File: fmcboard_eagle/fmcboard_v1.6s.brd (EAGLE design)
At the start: 147 x 74 mm, 294 parts, among them IC1 OPA699ID, IC10 LM358, IC11 7805DT, IC12 SN74AUC2G66DCTR, IC13 SN74AUC2G66DCTR, IC14 SN74AUC2G66DCTR, IC15 SN74AUC2G66DCTR, IC16 DAC7578SPWR, IC17 SN74AUC2G66DCTR, IC18 SN74AUC2G66DCTR, IC19 SN74AUC2G66DCTR, IC2 DAC7578SPWR, IC20 SN74AUC2G66DCTR, IC21 74AUP2GU04GW, IC22 74AUP2GU04GW, IC23 74AUP2GU04GW, IC24 74AUP2GU04GW, IC25 MC7905ACD2TR4G, IC26 AMS1117-1.8, IC27 LM358, IC28 SN74AUC2G66DCTR, IC29 LM337KVURG3, IC3 LTC6229IMS8E#TRPBF, IC30 SN74AUC2G66DCTR, IC31 SN74AUC2G66DCTR, IC32 SN74AUC2G66DCTR, IC33 LTC6229IMS8E#TRPBF, IC34 74AUP2GU04GW, IC35 74AUP2GU04GW, IC36 TPS5430DDAR, IC37 TPS5430DDAR, IC4 OPA695IDR, IC5 LTC6229IMS8E#TRPBF, IC6 OPA695IDR, IC7 OPA699ID, IC8 LM358, IC9 LM358, J1 8pin, J12 4p-2.54, J13 4p-2.54, J2 ASP-134604-01, J3 2p-2.54, J5 4p-2.54, J8 4p-2.54, J9 2p-2.54

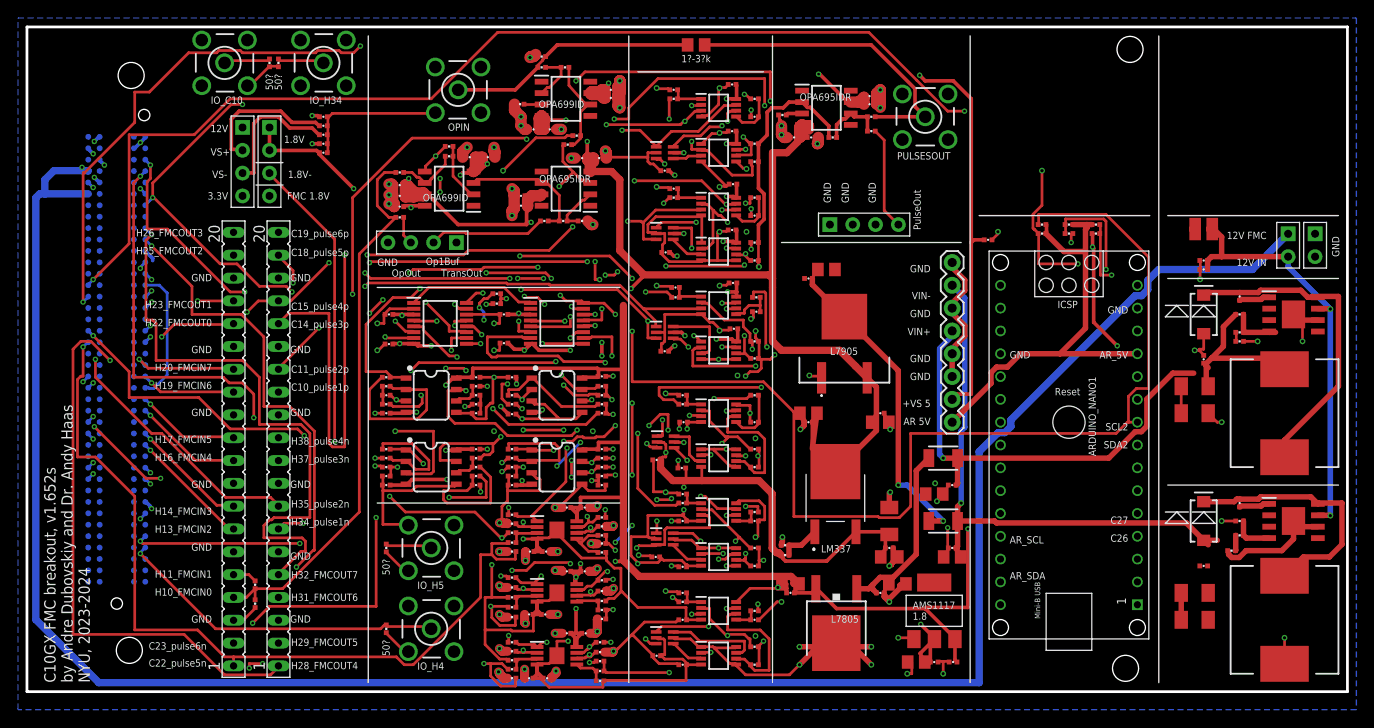
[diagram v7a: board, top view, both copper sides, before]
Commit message: 0805 10uF
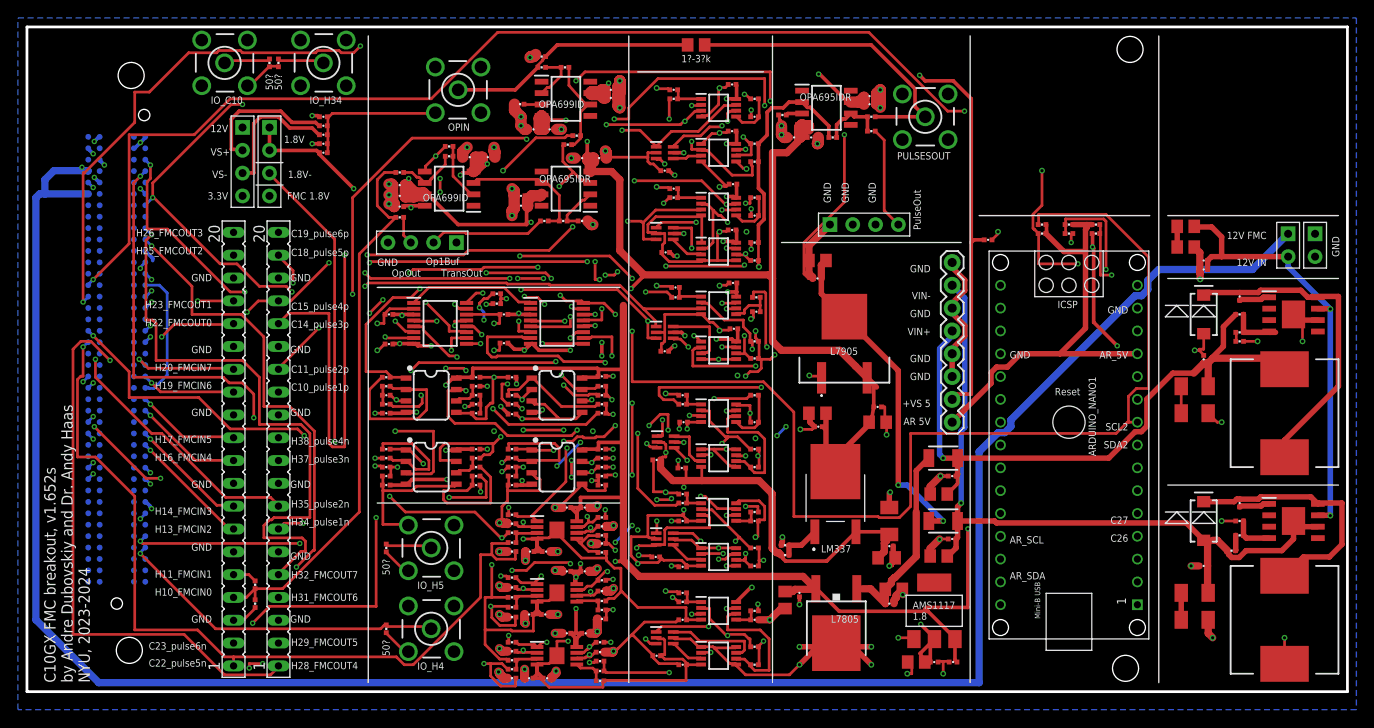
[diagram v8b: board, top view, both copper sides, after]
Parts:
- moved C120 2.50 mm to (129.0, 49.5)
- moved C64 2.01 mm to (129.0, 51.8)
- moved C38 1.90 mm to (84.4, 10.2), turned to 270 degrees
- moved C43 1.56 mm to (96.0, 9.80)
- moved C41 1.50 mm to (101.5, 15.1)
- moved C111 1.41 mm to (88.0, 48.0)
- moved C33 1.21 mm to (88.1, 29.5)
- moved C42 1.00 mm to (103.0, 24.0)
- moved C44 1.00 mm to (103.0, 17.0)
- moved C45 1.00 mm to (88.0, 46.0)
- moved C47 1.00 mm to (86.0, 11.0), turned to 270 degrees
- moved C77 1.00 mm to (88.0, 31.0)
- moved C25 0.76 mm to (94.7, 31.7)
- moved C110 0.72 mm to (96.5, 11.4)
- moved C1 0.50 mm to (101.5, 22.0)
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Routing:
- net GND: track 515.0 -> 625.9 mm, vias 124 -> 129
- net VIN+: track 70.2 -> 81.0 mm
- net VIN-: track 75.4 -> 83.8 mm
- net VIN+CLEAN: track 20.6 -> 27.4 mm
- net VS-: track 251.0 -> 244.8 mm
- net VS+: track 378.3 -> 384.0 mm
- net 1V8-: track 268.3 -> 271.8 mm
- net VIN-CLEAN: track 35.2 -> 37.0 mm
- net VIN: track 48.0 -> 49.6 mm
- net N$29: track 1.00 -> 2.30 mm
